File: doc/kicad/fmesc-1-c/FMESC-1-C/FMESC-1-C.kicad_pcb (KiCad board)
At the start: 2 copper layers, 14 x 21 mm, 43 parts, among them J1 Conn_01x02, J2 Conn_01x02, J3 Conn_01x02, J4 Conn_01x02, J5 Conn_01x02, J6 Conn_01x02, U1 FD6288Q

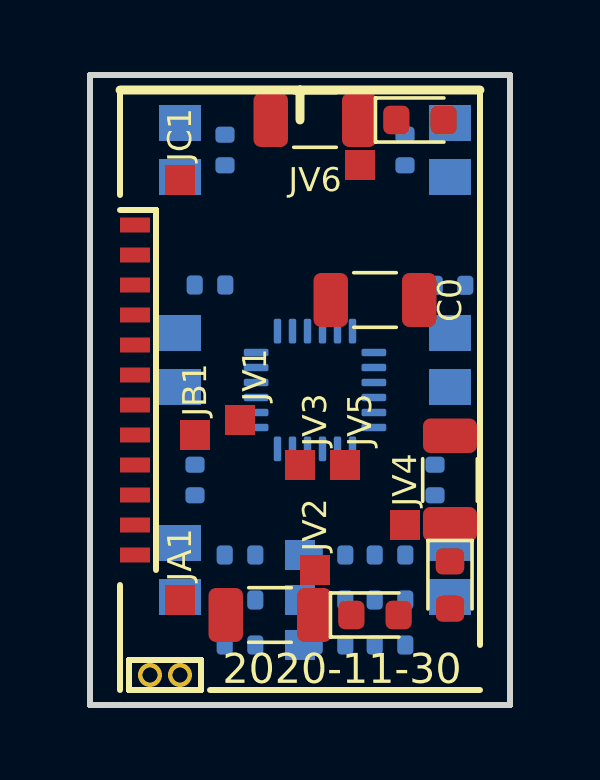
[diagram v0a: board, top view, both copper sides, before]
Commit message: doc/kicad: FMESC-1-C PCB v0.2
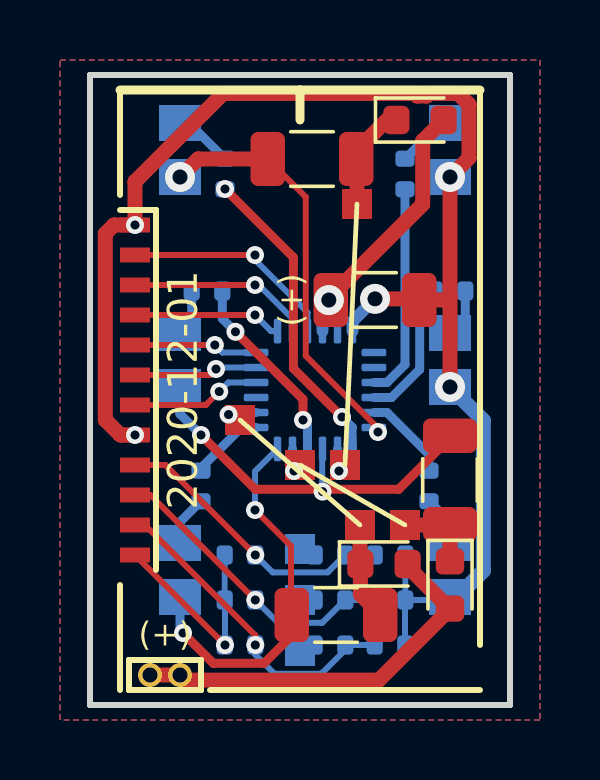
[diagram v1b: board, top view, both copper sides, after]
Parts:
- removed JA1, JB1, JC1: Conn_01x01, fmlibf:JS_1P_1x1mm
- moved C1 2.20 mm to (121.7, 72.0)
- moved JV2 2.12 mm to (122.5, 69.0)
- moved D1 1.73 mm to (123.3, 70.3)
- moved C3 1.30 mm to (120.9, 56.8)
- moved JV6 1.30 mm to (122.4, 58.3)
- moved R5 0.80 mm to (124.0, 57.3)
- moved R6 0.80 mm to (118.0, 57.3)
- moved R1 0.28 mm to (124.8, 67.7)
- moved R2 0.28 mm to (117.2, 67.7)
- moved R4 0.22 mm to (117.4, 61.2)
- moved JA2 0.20 mm to (120.5, 73.2)
- moved JC2 0.20 mm to (120.5, 69.8)
- moved R3 0.19 mm to (125.5, 61.2)
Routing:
- net GND: track 0.00 -> 48.7 mm, vias 0 -> 5
- net +BATT: track 0.00 -> 21.8 mm, vias 0 -> 1
- net /C1: track 0.00 -> 13.8 mm, vias 0 -> 2
- net /B1: track 0.00 -> 13.1 mm, vias 0 -> 2
- net /A1: track 0.00 -> 12.0 mm, vias 0 -> 2
- net /SA: track 0.00 -> 10.9 mm, vias 0 -> 1
- net /CHG: track 0.00 -> 10.4 mm, vias 0 -> 2
- net /SB: track 0.00 -> 10.1 mm, vias 0 -> 1
- net /SC: track 0.00 -> 9.72 mm, vias 0 -> 1
- net /GLC: track 0.00 -> 7.26 mm, vias 0 -> 1
- net /S0: track 0.00 -> 7.25 mm, vias 0 -> 1
- net /CLG: track 0.00 -> 7.14 mm
- net /BHG: track 0.00 -> 6.44 mm, vias 0 -> 2
- net /GLB: track 0.00 -> 6.13 mm, vias 0 -> 1
- net /GLA: track 0.00 -> 4.97 mm, vias 0 -> 1
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- added copper zone on B.Cu, net GND
- added copper zone on F.Cu, net GND
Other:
- board text added: "(+)"
- board text added: "2020-12-01"
- board text removed: "2020-11-30"

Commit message: doc/kicad: FMESC-1-C PCB move some
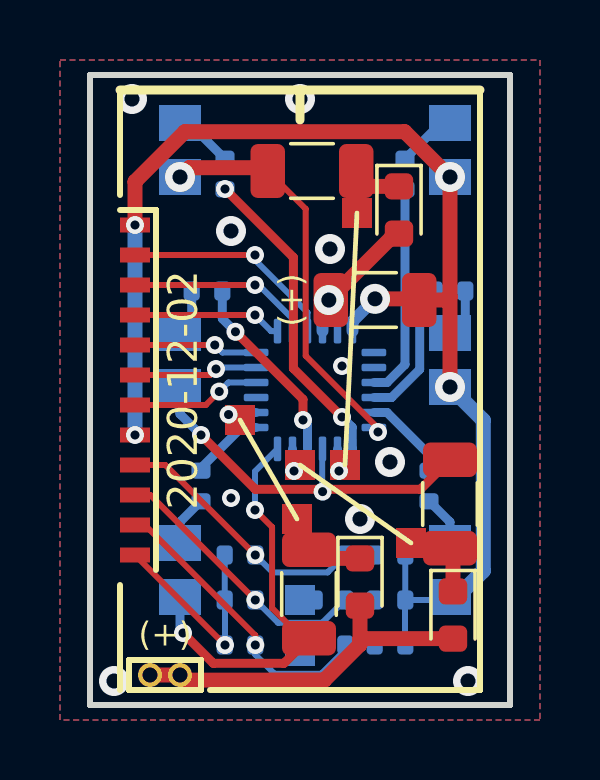
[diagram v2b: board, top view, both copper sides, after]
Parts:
- moved D3 3.08 mm to (123.8, 58.5), turned to 270 degrees
- moved JV2 2.11 mm to (120.4, 68.8)
- moved C1 1.14 mm to (120.8, 71.3), turned to 270 degrees
- moved D2 1.00 mm to (125.6, 72.0)
- moved D1 1.00 mm to (122.5, 70.9), turned to 270 degrees
- moved C2 0.80 mm to (125.5, 68.3)
- moved JV4 0.63 mm to (124.2, 69.6)
- moved C3 0.40 mm to (120.9, 57.2)
- moved JV6 0.30 mm to (122.4, 58.6)
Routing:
- net +BATT: track 21.8 -> 16.3 mm
- net GND: track 48.7 -> 43.7 mm, vias 5 -> 15
- net /A1: track 12.0 -> 13.2 mm
- net Net-(C3-Pad1): track 3.09 -> 2.39 mm
- net Net-(C1-Pad1): track 3.28 -> 2.69 mm
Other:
- board text added: "2020-12-02"
- board text removed: "2020-12-01"
